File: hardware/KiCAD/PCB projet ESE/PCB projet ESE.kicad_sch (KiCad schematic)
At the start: 46 parts, among them J1 Conn_01x06, J16 Conn_01x03, J2 Conn_01x04, J3 Conn_01x06, J4 Conn_01x06, J5 Conn_01x04, J6 Conn_01x02, J7 Conn_ST_STDC14, SW1 SW_SPST, SW2 472121010111, U1 ZXBM5210-SP, U2 ZXBM5210-SP, U3 STM32G474RETx, U4 ADXL343

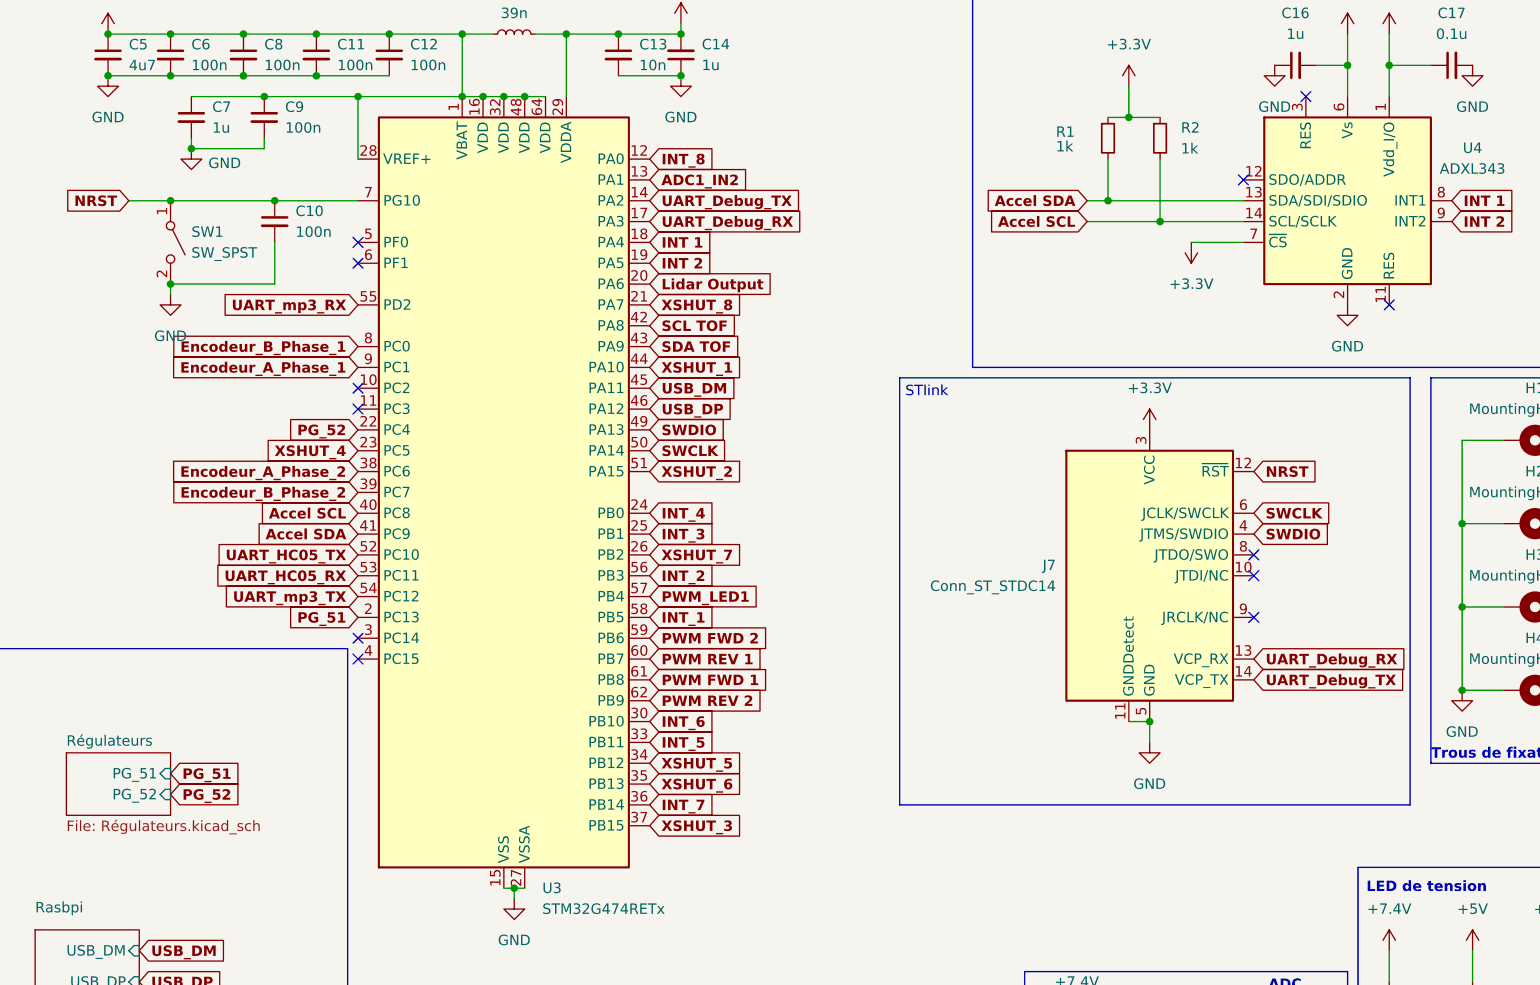
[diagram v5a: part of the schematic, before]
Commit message: modif pcb editor & sch for new uc pinout
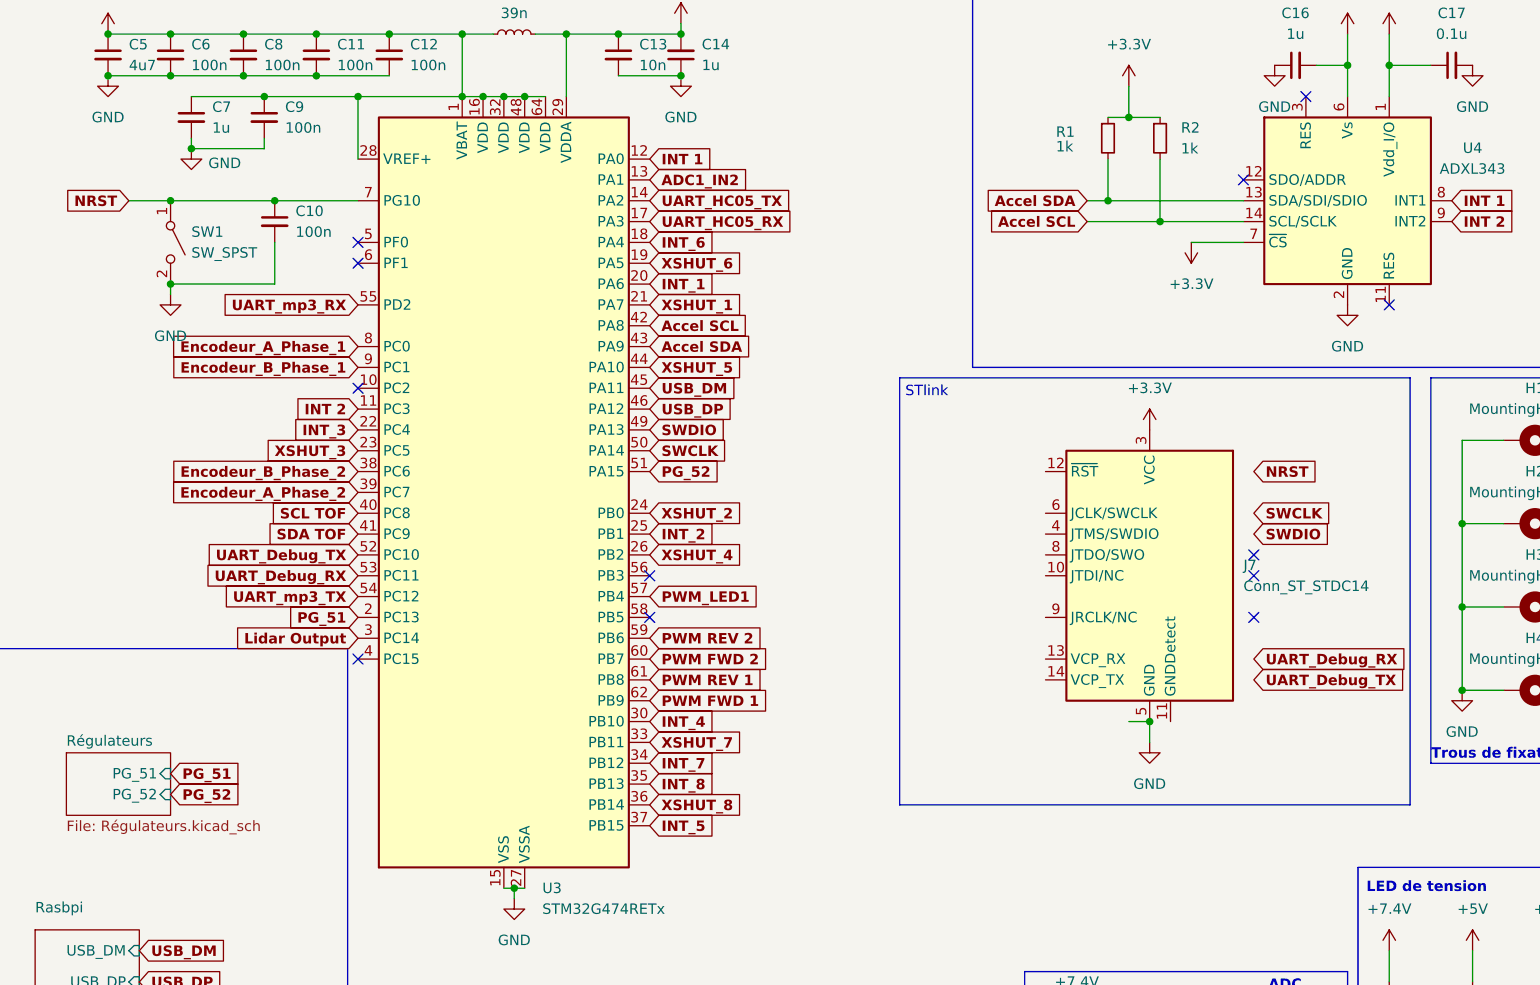
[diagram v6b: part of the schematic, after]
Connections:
- net Accel SCL: now also U3.42 (PA8); no longer U3.40 (PC8)
- net Accel SDA: now also U3.43 (PA9); no longer U3.41 (PC9)
- net Encodeur_A_Phase_1: now also U3.8 (PC0); no longer U3.9 (PC1)
- net Encodeur_A_Phase_2: now also U3.39 (PC7); no longer U3.38 (PC6)
- net Encodeur_B_Phase_1: now also U3.9 (PC1); no longer U3.8 (PC0)
- net Encodeur_B_Phase_2: now also U3.38 (PC6); no longer U3.39 (PC7)
- net GND: no longer J7.11 (GNDDetect)
- net INT 1: now also U3.12 (PA0); no longer U3.18 (PA4)
- net INT 2: now also U3.11 (PC3); no longer U3.19 (PA5)
- net INT_1: now also U3.20 (PA6); no longer U3.58 (PB5)
- net INT_2: now also U3.25 (PB1); no longer U3.56 (PB3)
- net INT_3: now also U3.22 (PC4); no longer U3.25 (PB1)
- net INT_4: now also U3.30 (PB10); no longer U3.24 (PB0)
- net INT_5: now also U3.37 (PB15); no longer U3.33 (PB11)
- net INT_6: now also U3.18 (PA4); no longer U3.30 (PB10)
- net INT_7: now also U3.34 (PB12); no longer U3.36 (PB14)
- net INT_8: now also U3.35 (PB13); no longer U3.12 (PA0)
- net Lidar Output : now also U3.3 (PC14); no longer U3.20 (PA6)
- net NRST: no longer J7.12 (~{RST})
- net PG_52: now also U3.51 (PA15); no longer U3.22 (PC4)
- net PWM FWD 1: now also U3.62 (PB9); no longer U3.61 (PB8)
- net PWM FWD 2: now also U3.60 (PB7); no longer U3.59 (PB6)
- net PWM REV 1: now also U3.61 (PB8); no longer U3.60 (PB7)
- net PWM REV 2: now also U3.59 (PB6); no longer U3.62 (PB9)
- net SCL TOF: now also U3.40 (PC8); no longer U3.42 (PA8)
- net SDA TOF: now also U3.41 (PC9); no longer U3.43 (PA9)
- net SWCLK: no longer J7.6 (JCLK/SWCLK)
- net SWDIO: no longer J7.4 (JTMS/SWDIO)
- net UART_Debug_RX: now also U3.53 (PC11); no longer J7.13 (VCP_RX), U3.17 (PA3)
- net UART_Debug_TX: now also U3.52 (PC10); no longer J7.14 (VCP_TX), U3.14 (PA2)
- net UART_HC05_RX: now also U3.17 (PA3); no longer U3.53 (PC11)
- net UART_HC05_TX: now also U3.14 (PA2); no longer U3.52 (PC10)
- net XSHUT_1: now also U3.21 (PA7); no longer U3.44 (PA10)
- net XSHUT_2: now also U3.24 (PB0); no longer U3.51 (PA15)
- net XSHUT_3: now also U3.23 (PC5); no longer U3.37 (PB15)
- net XSHUT_4: now also U3.26 (PB2); no longer U3.23 (PC5)
- net XSHUT_5: now also U3.44 (PA10); no longer U3.34 (PB12)
- net XSHUT_6: now also U3.19 (PA5); no longer U3.35 (PB13)
- net XSHUT_7: now also U3.33 (PB11); no longer U3.26 (PB2)
- net XSHUT_8: now also U3.36 (PB14); no longer U3.21 (PA7)
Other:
- moved on the sheet: J7

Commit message: maj
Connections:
- net GND: now also J7.11 (GNDDetect)
- net NRST: now also J7.12 (~{RST})
- net SWCLK: now also J7.6 (JCLK/SWCLK)
- net SWDIO: now also J7.4 (JTMS/SWDIO)
- net UART_Debug_RX: now also J7.13 (VCP_RX)
- net UART_Debug_TX: now also J7.14 (VCP_TX)
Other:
- moved on the sheet: J7
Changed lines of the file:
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@@
 		(on_board yes)
 		(dnp no)
-		(fields_autoplaced yes)
 		(property "Reference" "U3"
 			(at 152.0033 127 0)
@@
 		(lib_id "Connector:Conn_ST_STDC14")
 		(at 226.06 88.9 0)
-		(mirror y)
 		(unit 1)
 		(exclude_from_sim no)
@@
 		(dnp no)
 		(property "Reference" "J7"
-			(at 237.49 87.6299 0)
+			(at 214.63 87.6299 0)
 			(effects
 				(font
@@
 		)
 		(property "Value" "Conn_ST_STDC14"
-			(at 237.49 90.1699 0)
+			(at 214.63 90.1699 0)
 			(effects
 				(font
@@
 		)
 		(property "Datasheet" "https://www.st.com/content/ccc/resource/technical/document/user_manual/group1/99/49/91/b6/b2/3a/46/e5/DM00526767/files/DM00526767.pdf/jcr:content/translations/en.DM00526767.pdf"
-			(at 234.95 120.65 90)
+			(at 217.17 120.65 90)
 			(effects
 				(font

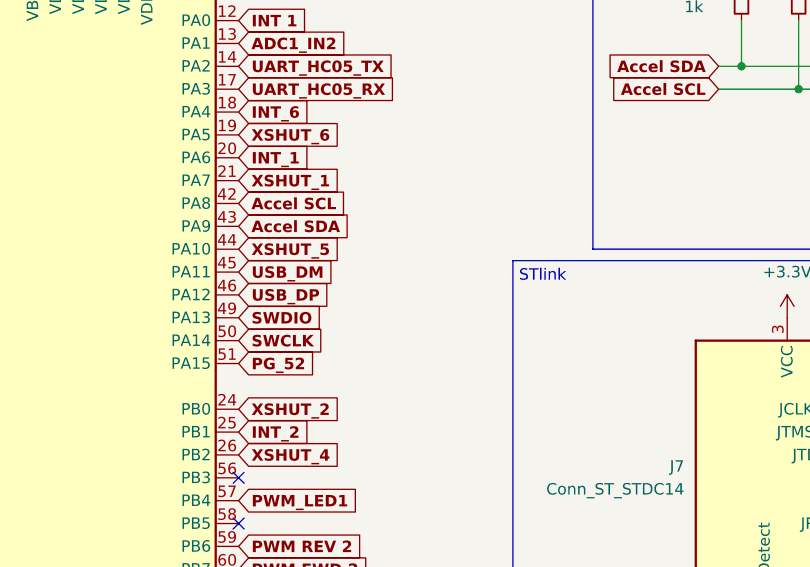
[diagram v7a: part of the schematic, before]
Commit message: replace usb c by jst xh
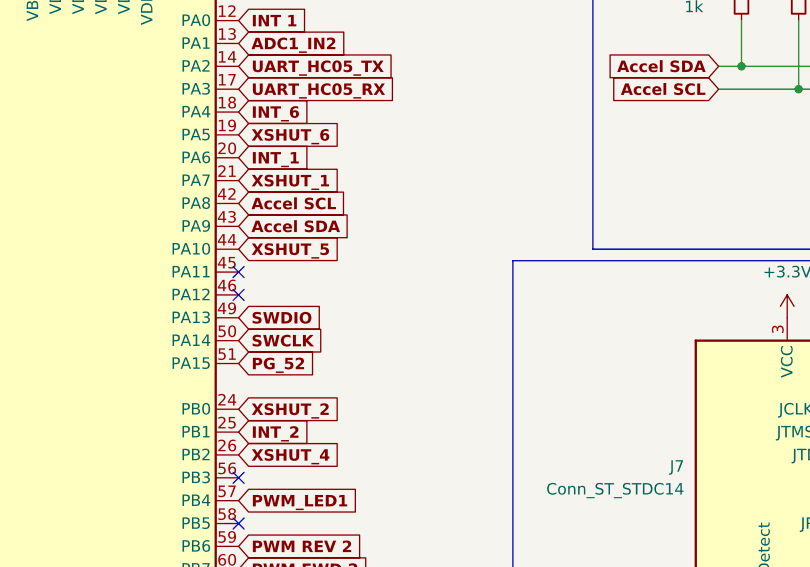
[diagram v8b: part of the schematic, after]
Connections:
- net USB_DM: no longer U3.45 (PA11)
- net USB_DP: no longer U3.46 (PA12)
- no-connect marks 15 -> 17
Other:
- note removed: "STlink"
